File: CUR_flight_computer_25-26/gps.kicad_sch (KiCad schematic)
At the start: 11 parts, among them U11 SAM-M8Q

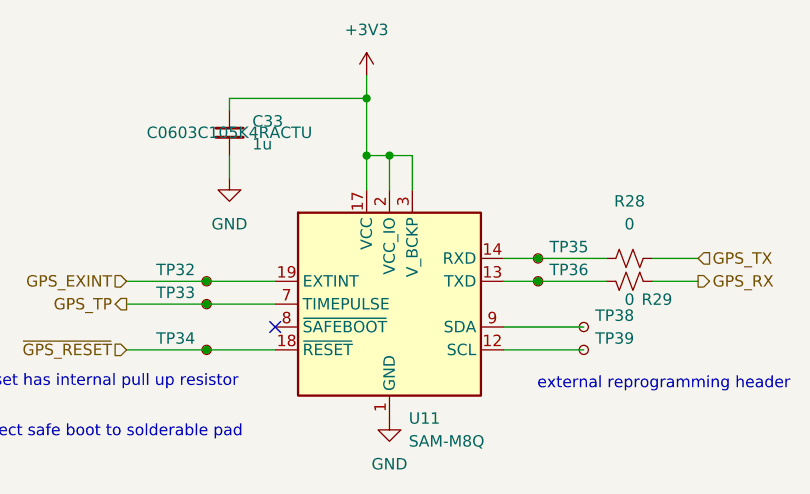
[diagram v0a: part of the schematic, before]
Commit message: Add MPNs for ICs
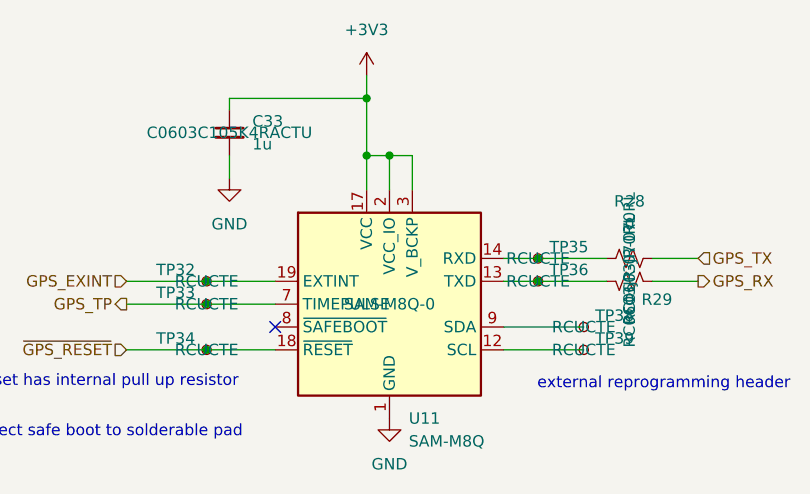
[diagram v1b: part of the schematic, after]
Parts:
- R28, R29: MPN (none) -> RC0603JR-070RL
- TP32, TP33, TP34, TP35, TP36, TP38, TP39: value TestPoint_Small -> RCUCTE; MPN (none) -> RCUCTE
- U11: MPN (none) -> SAM-M8Q-0
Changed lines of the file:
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@@
 			)
 		)
-		(property "Value" "TestPoint_Small"
+		(property "Value" "RCUCTE"
 			(at 92.71 49.5299 0)
 			(effects
@@
 			)
 		)
+		(property "MPN" "RCUCTE"
+			(at 91.44 48.26 0)
+			(effects
+				(font
+					(size 1.27 1.27)
+				)
+			)
+		)
 		(pin "1"
 		)
@@
 			)
 		)
-		(property "Value" "TestPoint_Small"
+		(property "Value" "RCUCTE"
 			(at 92.71 52.0699 0)
 			(effects
@@
 			)
 		)
+		(property "MPN" "RCUCTE"
+			(at 91.44 50.8 0)
+			(effects
+				(font
+					(size 1.27 1.27)
+				)
+			)
+		)
 		(pin "1"
 		)
@@
 			)
 		)
-		(property "Value" "TestPoint_Small"
+		(property "Value" "RCUCTE"
 			(at 97.79 59.6899 0)
 			(effects
@@
 				)
 				(hide yes)
+			)
+		)
+		(property "MPN" "RCUCTE"
+			(at 96.52 58.42 0)
+			(effects
+				(font
+					(size 1.27 1.27)
+				)
 			)
 		)
@@
 			)
 		)
+		(property "MPN" "RC0603JR-070RL"
+			(at 101.6 50.8 0)
+			(effects
+				(font
+					(size 1.27 1.27)
+				)
+			)
+		)
 		(pin "1"
 		)
@@
 			)
 		)
+		(property "MPN" "RC0603JR-070RL"
+			(at 101.6 48.26 0)
+			(effects
+				(font
+					(size 1.27 1.27)
+				)
+			)
+		)
 		(pin "1"
 		)
@@
 				)
 				(hide yes)
+			)
+		)
+		(property "MPN" "SAM-M8Q-0"
+			(at 74.93 53.34 0)
+			(effects
+				(font
+					(size 1.27 1.27)
+				)
 			)
 		)
@@
 			)
 		)
-		(property "Value" "TestPoint_Small"
+		(property "Value" "RCUCTE"
 			(at 53.34 52.0699 0)
 			(effects
@@
 				)
 				(hide yes)
+			)
+		)
+		(property "MPN" "RCUCTE"
+			(at 54.61 50.8 0)
+			(effects
+				(font
+					(size 1.27 1.27)
+				)
 			)
 		)
@@
 			)
 		)
-		(property "Value" "TestPoint_Small"
+		(property "Value" "RCUCTE"
 			(at 53.34 59.6899 0)
 			(effects
@@
 				)
 				(hide yes)
+			)
+		)
+		(property "MPN" "RCUCTE"
+			(at 54.61 58.42 0)
+			(effects
+				(font
+					(size 1.27 1.27)
+				)
 			)
 		)
@@
 			)
 		)
-		(property "Value" "TestPoint_Small"
+		(property "Value" "RCUCTE"
 			(at 53.34 54.6099 0)
 			(effects
@@
 			)
 		)
+		(property "MPN" "RCUCTE"
+			(at 54.61 53.34 0)
+			(effects
+				(font
+					(size 1.27 1.27)
+				)
+			)
+		)
 		(pin "1"
 		)
@@
 			)
 		)
-		(property "Value" "TestPoint_Small"
+		(property "Value" "RCUCTE"
 			(at 97.79 57.1499 0)
 			(effects
@@
 			)
 		)
+		(property "MPN" "RCUCTE"
+			(at 96.52 55.88 0)
+			(effects
+				(font
+					(size 1.27 1.27)
+				)
+			)
+		)

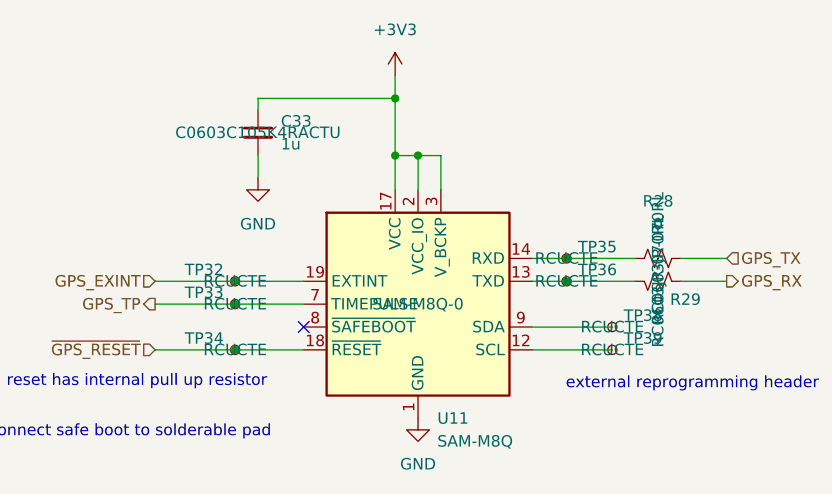
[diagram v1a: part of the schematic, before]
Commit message: Hide MPNs
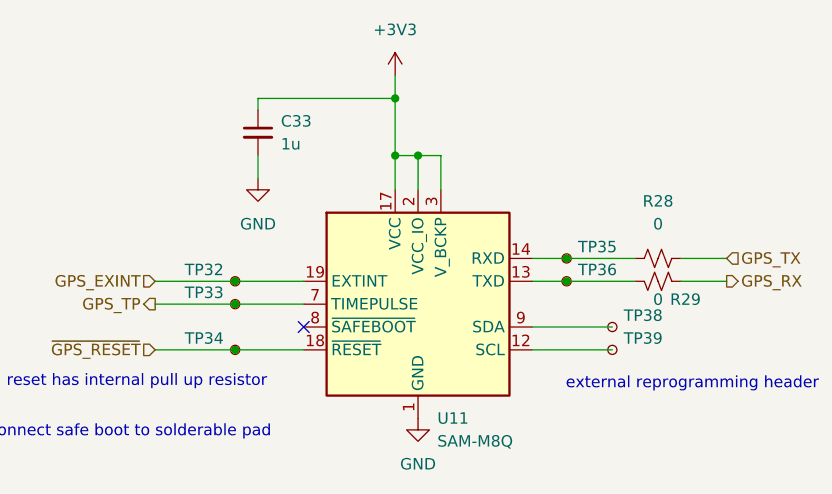
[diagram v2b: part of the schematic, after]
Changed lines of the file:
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@@
 					(size 1.27 1.27)
 				)
+				(hide yes)
 			)
 		)
@@
 					(size 1.27 1.27)
 				)
+				(hide yes)
 			)
 		)
@@
 					(size 1.27 1.27)
 				)
+				(hide yes)
 			)
 		)
@@
 					(size 1.27 1.27)
 				)
+				(hide yes)
 			)
 		)
@@
 					(size 1.27 1.27)
 				)
+				(hide yes)
 			)
 		)
@@
 					(size 1.27 1.27)
 				)
+				(hide yes)
 			)
 		)
@@
 					(size 1.27 1.27)
 				)
+				(hide yes)
 			)
 		)
@@
 					(size 1.27 1.27)
 				)
+				(hide yes)
 			)
 		)
@@
 					(size 1.27 1.27)
 				)
+				(hide yes)
 			)
 		)
@@
 					(size 1.27 1.27)
 				)
+				(hide yes)
 			)
 		)
@@
 					(size 1.27 1.27)
 				)
-			)
-		)
+				(hide yes)
+			)
+		)

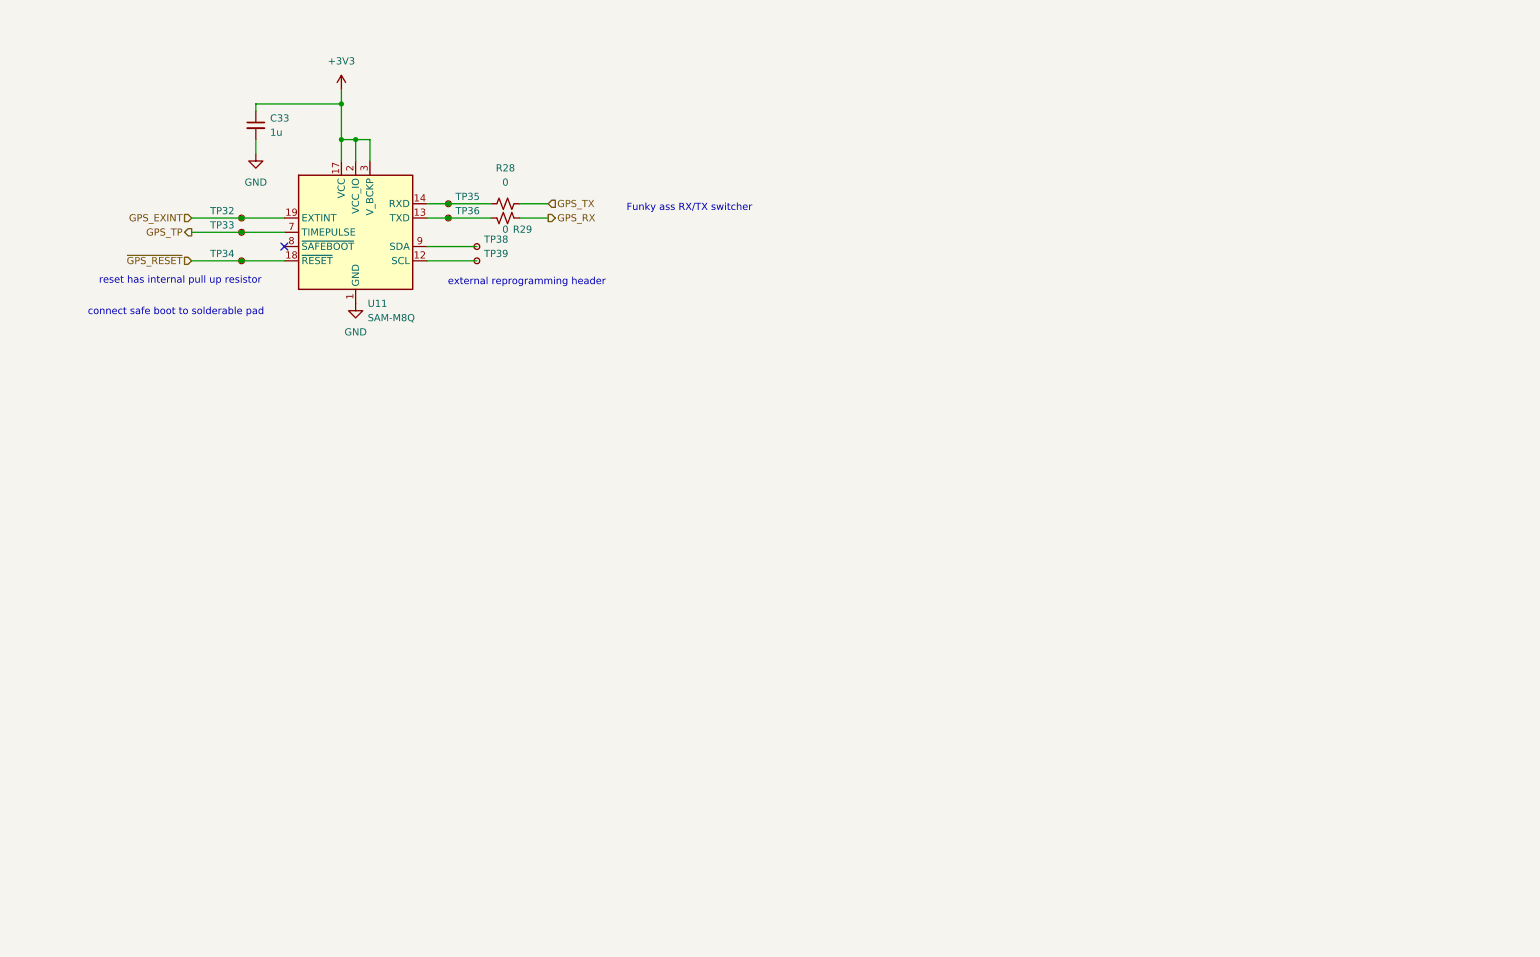
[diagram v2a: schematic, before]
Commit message: Cleaned up schematic
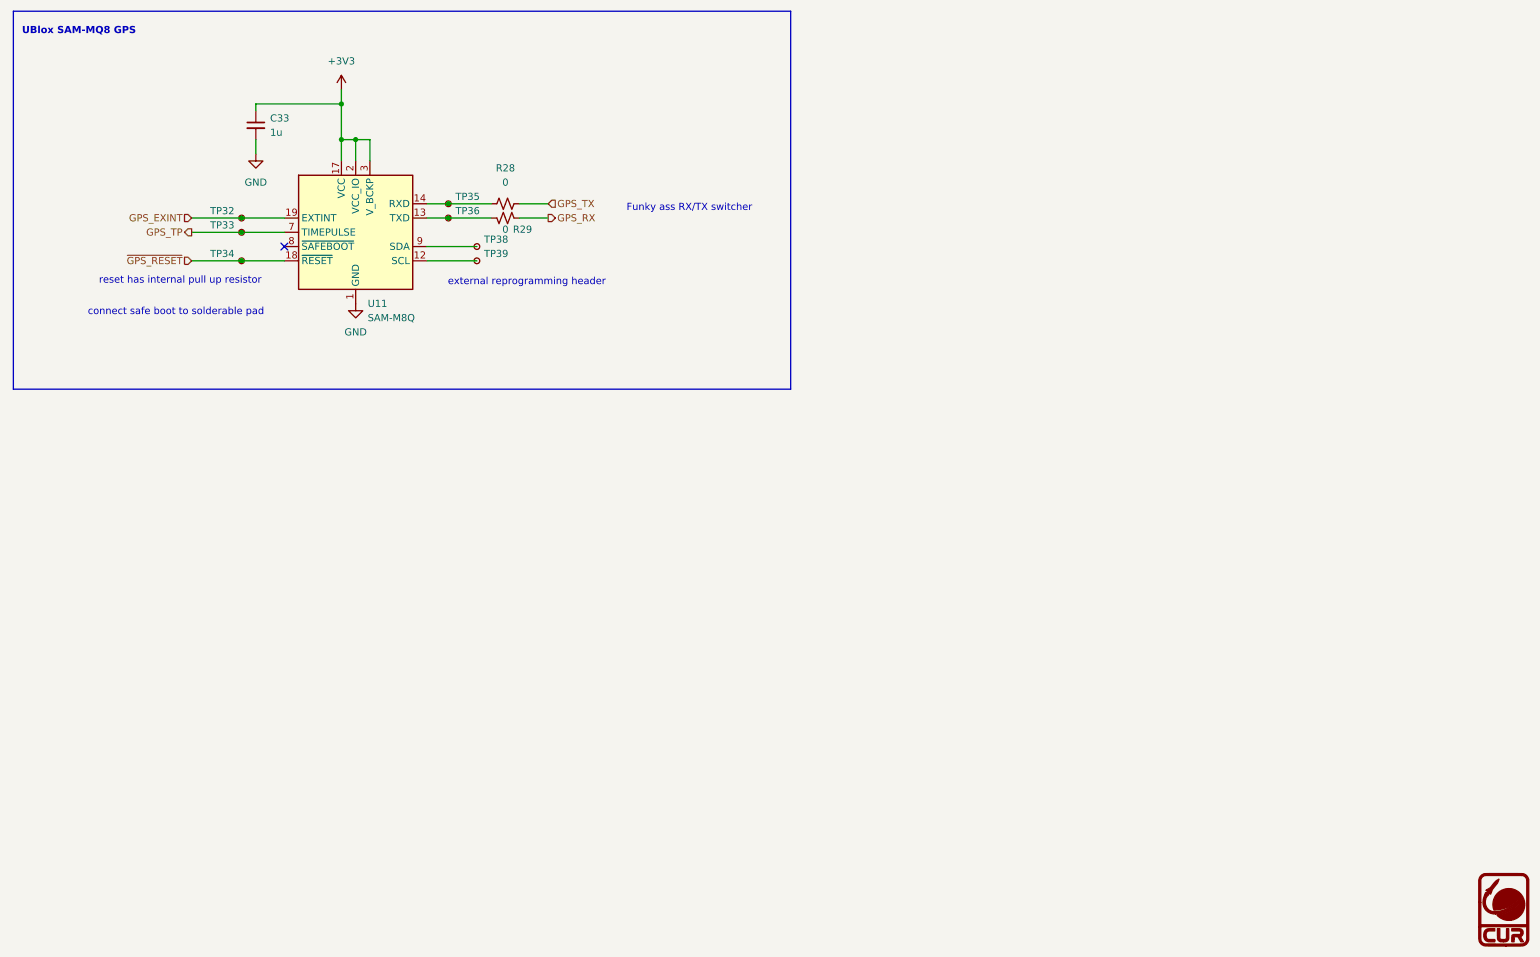
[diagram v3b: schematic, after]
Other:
- note added: "UBlox SAM-MQ8 GPS"
- company: (none) -> Clarkson University Rocketry
- title: (none) -> Flight Computer
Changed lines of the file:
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@@
 	(generator_version "9.0")
 	(paper "A4")
+	(title_block
+		(title "Flight Computer")
+		(date "2026-03-18")
+		(company "Clarkson University Rocketry")
+	)
+	(rectangle
+		(start 13.97 13.97)
+		(end 152.4 81.28)
+		(stroke
+			(width 0)
+			(type default)
+		)
+		(fill
+			(type none)
+		)
+	)
+	(text "UBlox SAM-MQ8 GPS"
+		(exclude_from_sim no)
+		(at 25.654 17.526 0)
+		(effects
+			(font
+				(size 1.27 1.27)
+				(thickness 0.254)
+				(bold yes)
+			)
+		)
+	)
 	(text "external reprogramming header\n"
 		(exclude_from_sim no)
@@
 					(unit 1)
 				)
+			)
+		)
+	)
+	(symbol
+		(lib_id "CUR_Logo:LOGO")
+		(at 279.4 173.99 0)
+		(unit 1)
+		(exclude_from_sim no)
+		(in_bom yes)
+		(on_board yes)
+		(dnp no)
+		(fields_autoplaced yes)
+		(property "Reference" "#G8"
+			(at 279.4 167.002 0)
+			(effects
+				(font
+					(size 1.27 1.27)
+				)
+				(hide yes)
+			)
+		)
+		(property "Value" "LOGO"
+			(at 279.4 180.978 0)
+			(effects
+				(font
+					(size 1.27 1.27)
+				)
+				(hide yes)
+			)
+		)
+		(property "Footprint" ""
+			(at 279.4 173.99 0)
+			(effects
+				(font
+					(size 1.27 1.27)
+				)
+				(hide yes)
+			)
+		)
+		(property "Datasheet" ""
+			(at 279.4 173.99 0)
+			(effects
+				(font
+					(size 1.27 1.27)
+				)
+				(hide yes)
+			)
+		)
+		(property "Description" ""
+			(at 279.4 173.99 0)
+			(effects
+				(font
+					(size 1.27 1.27)
+				)
+				(hide yes)
+			)
+		)
+		(instances
+			(project "CUR_flight_computer_25-26"
+				(path "/bf7761cc-1b32-4d86-809c-5f027005229b/e838d24c-cb75-4a46-b88f-e4466a269629"
+					(reference "#G8")
+					(unit 1)
+				)

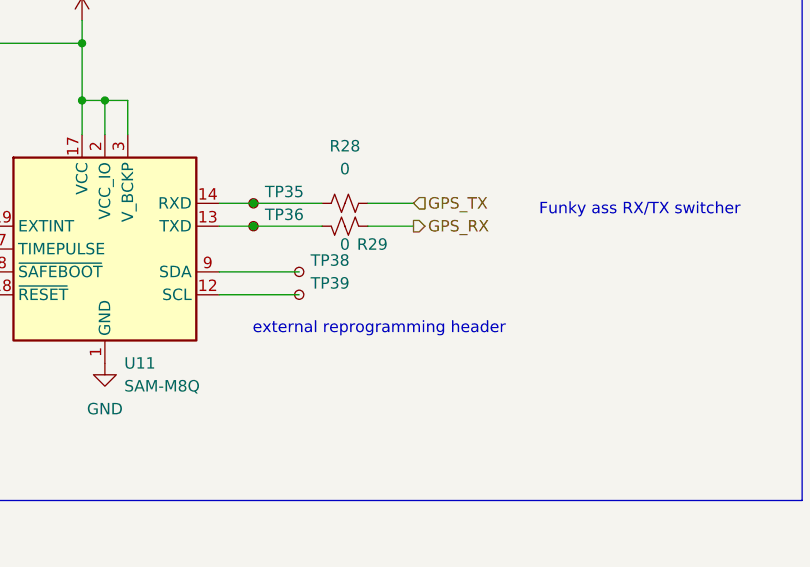
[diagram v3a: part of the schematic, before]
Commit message: Connect GPS I2C to LCD I2C
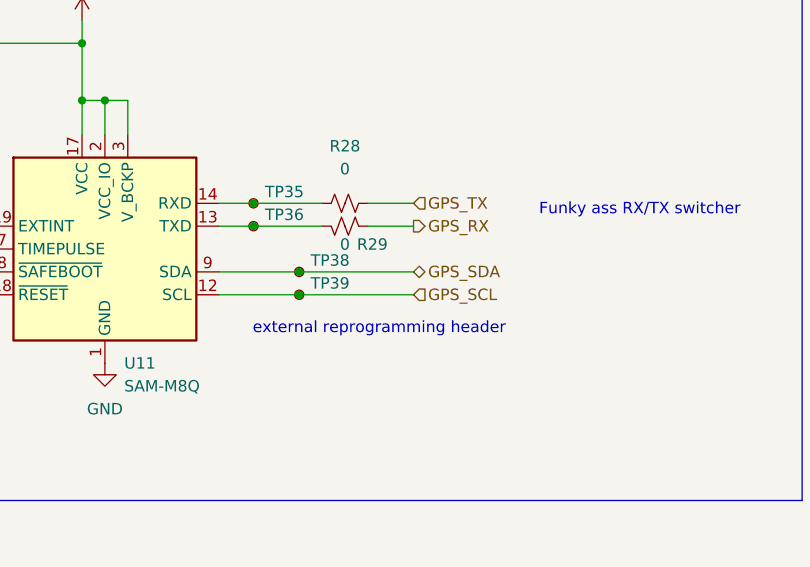
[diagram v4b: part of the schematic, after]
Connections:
- net GPS_SCL: now reaches TP39.1, U11.12 (SCL)
- net GPS_SDA: now reaches TP38.1, U11.9 (SDA)
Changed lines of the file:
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@@
+	)
+	(junction
+		(at 96.52 58.42)
+		(diameter 0)
+		(color 0 0 0 0)
 	)
 	(junction
@@
 	(junction
 		(at 91.44 48.26)
+		(diameter 0)
+		(color 0 0 0 0)
+	)
+	(junction
+		(at 96.52 55.88)
 		(diameter 0)
 		(color 0 0 0 0)
@@
 	(wire
 		(pts
+			(xy 96.52 55.88) (xy 109.22 55.88)
+		)
+		(stroke
+			(width 0)
+			(type default)
+		)
+	)
+	(wire
+		(pts
 			(xy 72.39 36.83) (xy 72.39 40.64)
 		)
@@
 		(pts
 			(xy 72.39 27.94) (xy 72.39 30.48)
+		)
+		(stroke
+			(width 0)
+			(type default)
+		)
+	)
+	(wire
+		(pts
+			(xy 96.52 58.42) (xy 109.22 58.42)
 		)
 		(stroke
@@
 		)
 	)
+	(hierarchical_label "GPS_SDA"
+		(shape bidirectional)
+		(at 109.22 55.88 0)
+		(effects
+			(font
+				(size 1.27 1.27)
+			)
+			(justify left)
+		)
+	)
 	(hierarchical_label "GPS_TP"
 		(shape output)
@@
 		)
 	)
+	(hierarchical_label "GPS_SCL"
+		(shape input)
+		(at 109.22 58.42 0)
+		(effects
+			(font
+				(size 1.27 1.27)
+			)
+			(justify left)
+		)
+	)

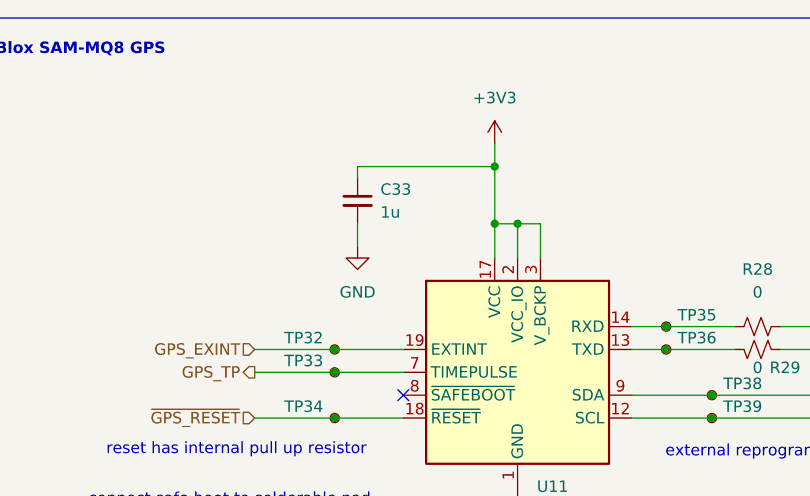
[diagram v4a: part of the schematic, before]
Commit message: BOM optimize 1u to 2.2u
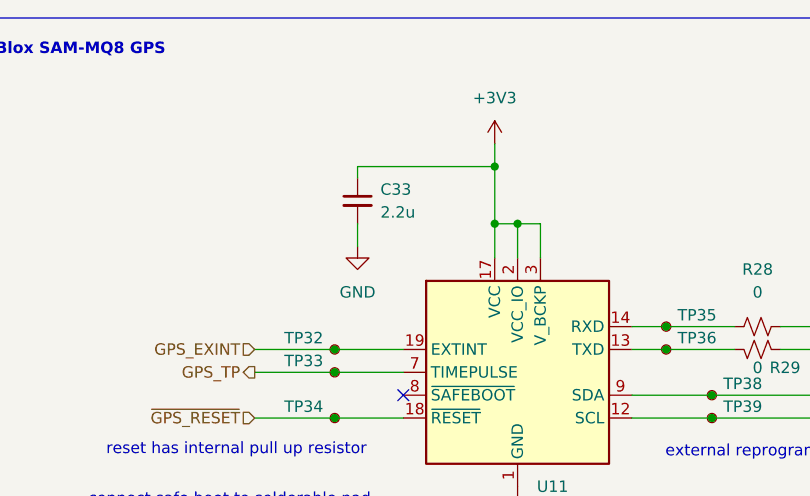
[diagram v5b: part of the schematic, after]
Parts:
- C33: value 1u -> 2.2u; MPN C0603C105K4RACTU -> CL10B225KP8NNNC
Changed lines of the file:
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@@
 			)
 		)
-		(property "Value" "1u"
+		(property "Value" "2.2u"
 			(at 59.69 35.5662 0)
 			(effects
@@
 			)
 		)
-		(property "MPN" "C0603C105K4RACTU"
+		(property "MPN" "CL10B225KP8NNNC"
 			(at 57.15 34.29 0)
 			(effects

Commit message: update sensors
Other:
- note removed: "Funky ass RX/TX switcher"
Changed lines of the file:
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@@
-		)
-	)
-	(text "Funky ass RX/TX switcher"
-		(exclude_from_sim no)
-		(at 134.366 49.022 0)
-		(effects
-			(font
-				(size 1.27 1.27)
-			)
 		)
 	)
